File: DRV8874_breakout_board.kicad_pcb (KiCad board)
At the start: 2 copper layers, 11 parts, among them U1 DRV8874PWPR

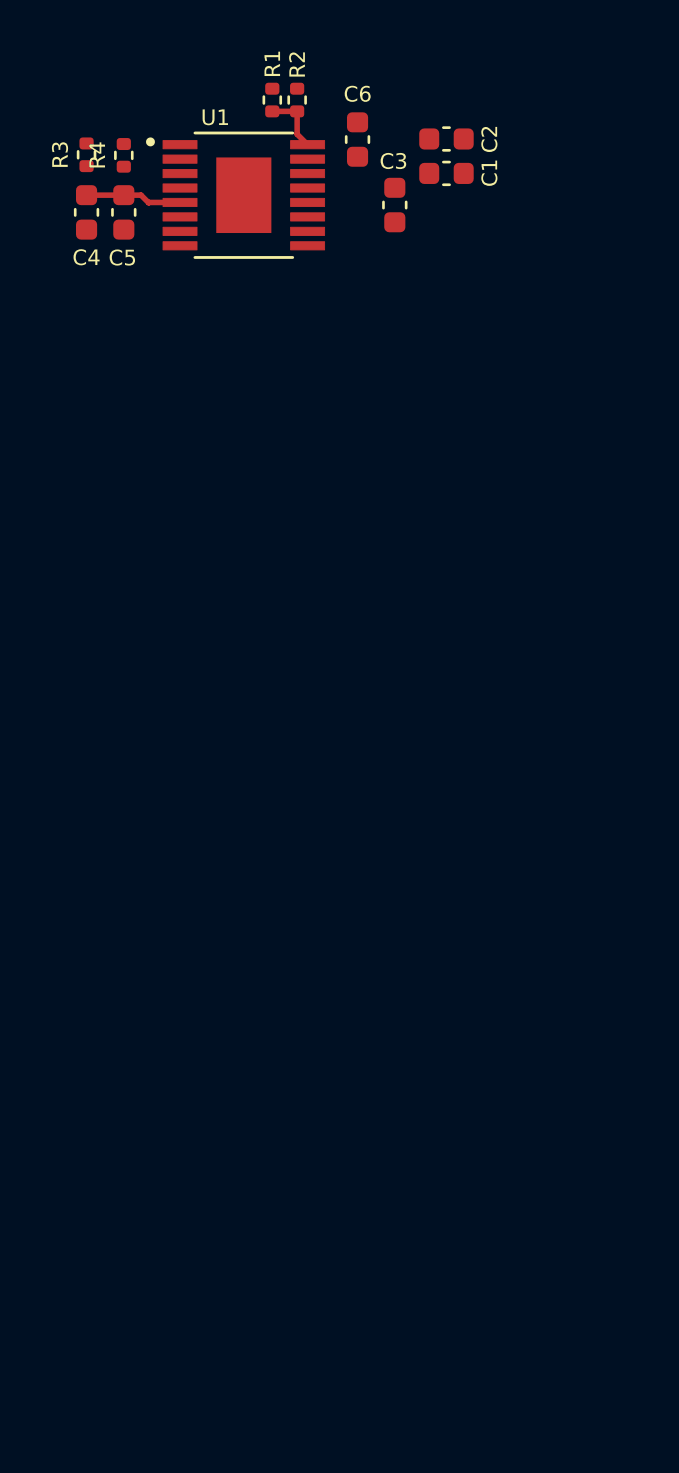
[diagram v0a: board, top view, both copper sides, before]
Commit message: Forma de PCB con espacios para tira de pines
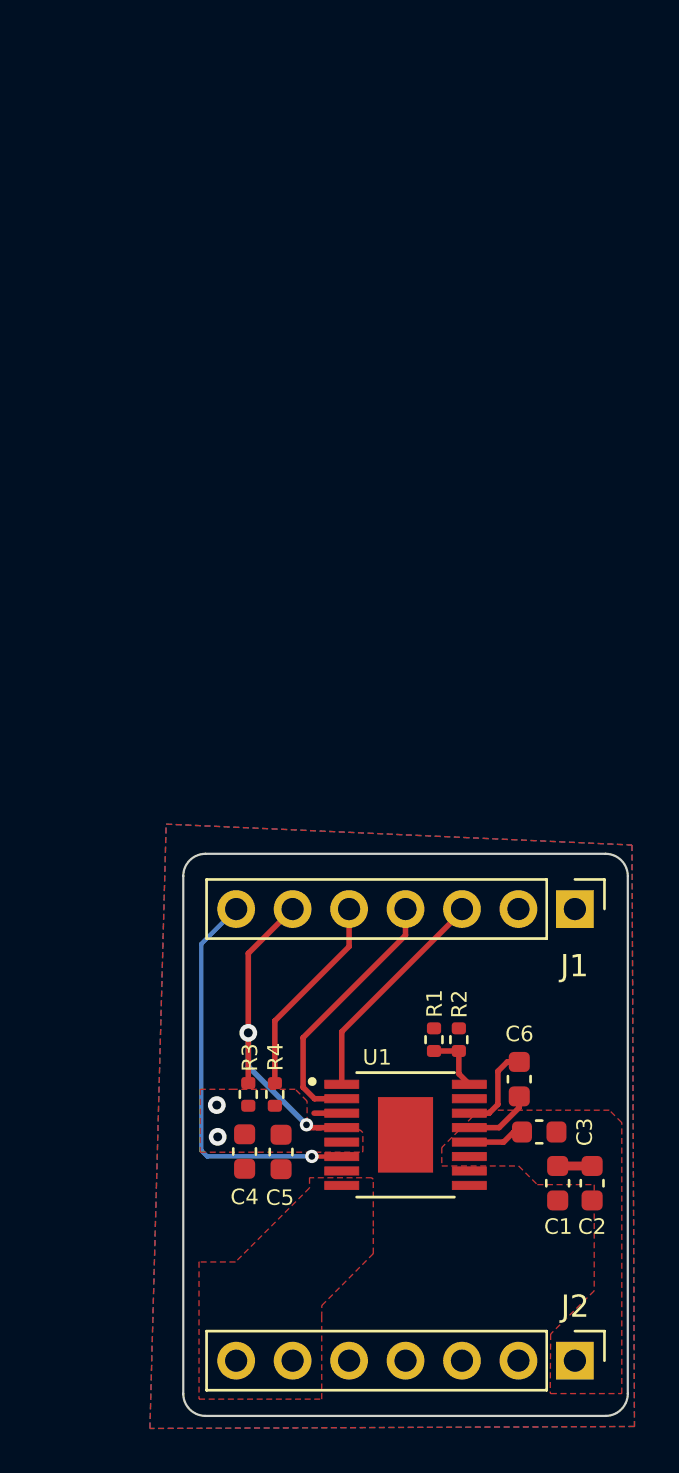
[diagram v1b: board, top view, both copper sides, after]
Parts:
- added J1: Conn1x7, Connector_PinHeader_2.54mm:PinHeader_1x07_P2.54mm_Vertical, F.Cu at (134.6, 104.1)
- added J2: Conn1x7, Connector_PinHeader_2.54mm:PinHeader_1x07_P2.54mm_Vertical, F.Cu at (134.6, 124.5)
- moved C2 47.4 mm to (135.4, 116.5), turned to -90 degrees
- moved C1 45.7 mm to (133.8, 116.5), turned to -90 degrees
- moved C6 42.9 mm to (132.1, 111.8)
- moved R1 42.9 mm to (128.3, 110.0)
- moved R2 42.9 mm to (129.4, 110.0)
- moved R3 42.9 mm to (119.9, 112.5)
- moved U1 42.9 mm to (127.0, 114.3)
- moved C5 42.9 mm to (121.4, 115.1)
- moved C4 42.8 mm to (119.8, 115.0)
- moved R4 42.8 mm to (121.1, 112.5)
- moved C3 42.2 mm to (133.0, 114.2), turned to 180 degrees
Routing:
- net /CurrADC: track 0.00 -> 17.9 mm, vias 0 -> 1
- net /nFault: track 0.00 -> 15.5 mm, vias 0 -> 2
- net /DIR: track 0.00 -> 11.9 mm
- net /nSleep: track 0.00 -> 10.5 mm
- net /PWM: track 0.00 -> 10.1 mm
- net +3V3: track 4.35 -> 0.00 mm, vias 0 -> 2
- net Net-(U1-CPL): track 0.00 -> 4.07 mm
- net Net-(U1-CPH): track 0.00 -> 3.12 mm
- net Net-(U1-VCP): track 0.00 -> 2.56 mm
- net Vdrive: track 0.00 -> 1.63 mm
- added copper zone on F.Cu, net +3V3
- added copper zone on F.Cu, net /M+
- added copper zone on B.Cu, net GND
- added copper zone on F.Cu, net GND
- added copper zone on F.Cu, net Vdrive
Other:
- board outline added: 20 x 25.3 mm

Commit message: primera iteración PCB
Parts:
- added R5: 62K, Resistor_SMD:R_0402_1005Metric, F.Cu at (120.4, 117.5)
- added R6: 0, Resistor_SMD:R_0402_1005Metric, F.Cu at (118.2, 116.5)
- added U2: Logo_Small, Herranz - Various:LOGO_small, B.Cu at (127.1, 118.2)
- moved C2 3.60 mm to (135.4, 112.9), turned to 90 degrees
- moved C1 1.45 mm to (134.6, 117.7), turned to 180 degrees
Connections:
- U1 pad 17: (no net) -> GND
- U1 pad 7: GND -> Net-(U1-IMODE)
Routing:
- net +3V3: track 0.00 -> 24.5 mm, vias 2 -> 3
- net Net-(U1-IMODE): track 0.00 -> 3.90 mm
- net GND: track 0.00 -> 2.49 mm, vias 0 -> 6
- net /nSleep: track 10.5 -> 12.8 mm
- net Vdrive: track 1.63 -> 0.00 mm
- net /CurrADC: track 17.9 -> 19.2 mm, vias 1 -> 2
- added copper zone on F.Cu, net /M-
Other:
- board text added: "11-2023"
- board text added: "CERN-OHL-W"
- board text added: "DVR8874 PCB01"

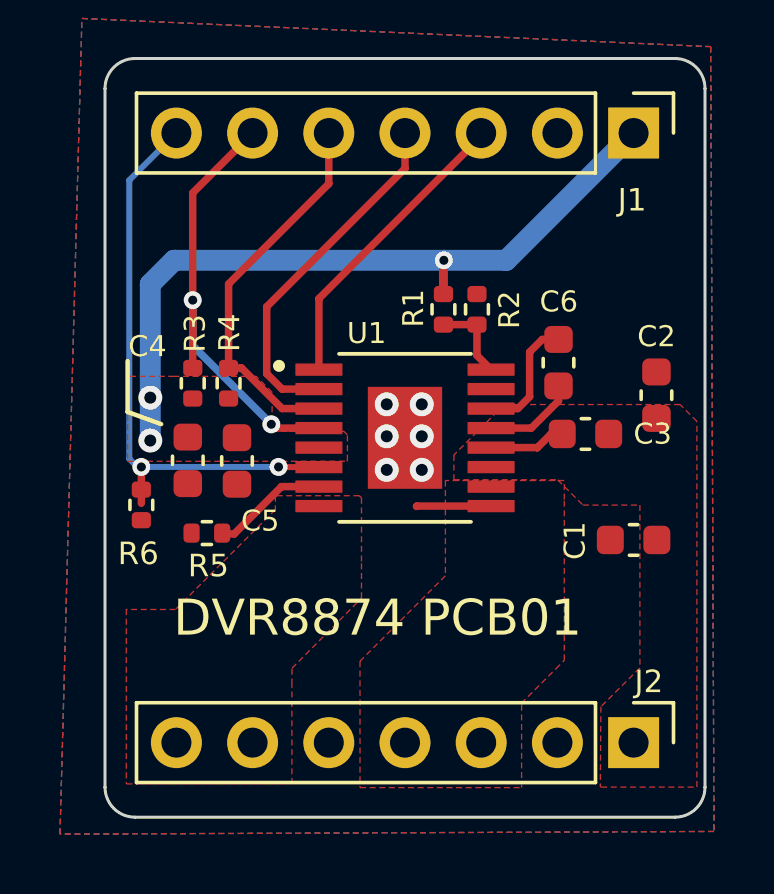
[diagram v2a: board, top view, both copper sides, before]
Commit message: Añadido divisor de resistencia para v_ref
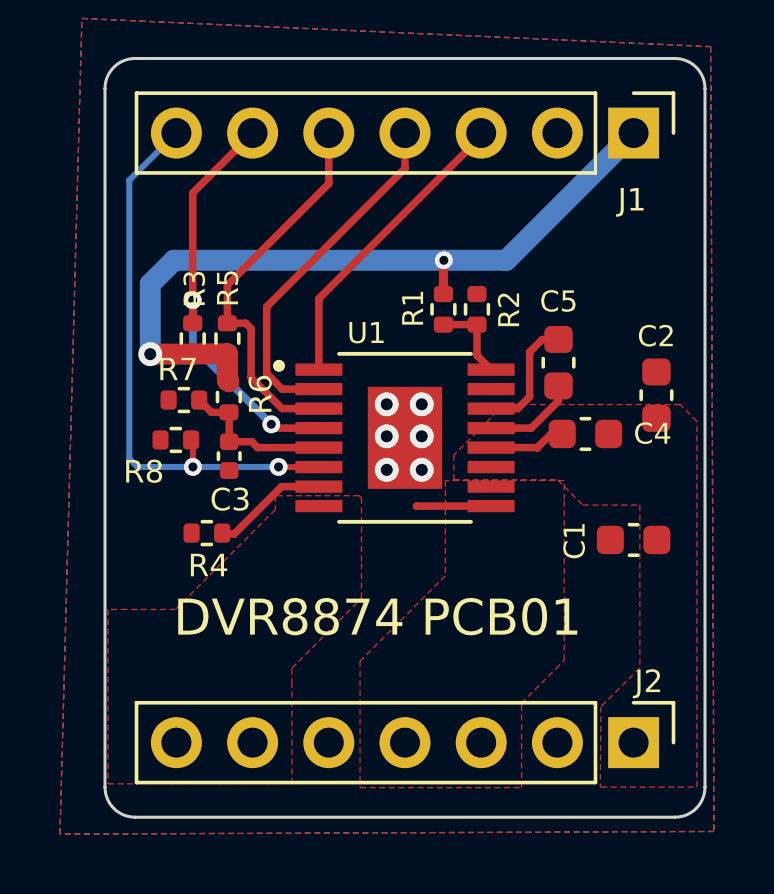
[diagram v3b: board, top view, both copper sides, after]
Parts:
- removed the C4 at (119.8, 115.0)
- removed the C5 at (121.4, 115.1)
- added C3: Gen_C, Capacitor_SMD:C_0402_1005Metric, F.Cu at (121.1, 114.9)
- added R6: 0, Resistor_SMD:R_0402_1005Metric, F.Cu at (121.1, 112.9)
- added R7: 0, Resistor_SMD:R_0402_1005Metric, F.Cu at (119.6, 113.0)
- moved R8 2.45 mm to (119.4, 114.4), turned to 0 degrees
- moved R5 1.49 mm to (121.1, 111.0)
- moved R3 1.49 mm to (119.9, 111.0)
- renumbered C3 to C4, C6 to C5, R5 to R4, R4 to R5, R6 to R8
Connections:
- U1 pad 17: GND -> (no net)
- U1 pad 5: +3V3 -> Net-(U1-VREF)
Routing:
- net Net-(U1-VREF): track 0.00 -> 5.21 mm
- net /nFault: track 15.5 -> 14.0 mm
- net +3V3: track 24.5 -> 25.2 mm, vias 3 -> 2
- removed copper zone on F.Cu, net +3V3
